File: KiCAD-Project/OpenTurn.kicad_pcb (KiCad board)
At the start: 4 copper layers, 90 x 90 mm, 152 parts, among them J201 XT30, J202 XT30, J203 TLE2, J204 CAN, J205 CAN, J301 GPIOs, J302 JTAG/SW, Q501 IAUC120N06S5N017ATMA1, Q502 IAUC120N06S5N017ATMA1, Q601 IAUC120N06S5N017ATMA1, Q602 IAUC120N06S5N017ATMA1, Q701 IAUC120N06S5N017ATMA1, Q702 IAUC120N06S5N017ATMA1, U201 TI_TCAN337G, U202 TLE5012B_E1000, U203 MAX15062A, U301 CY8C6244AZI-S4D92, U302 MCP9700AT-HTT, U303 MCP9700AT-HTT, U401 DRV8323SRTAR-DRV8323SRTAR, Y301 32MHz

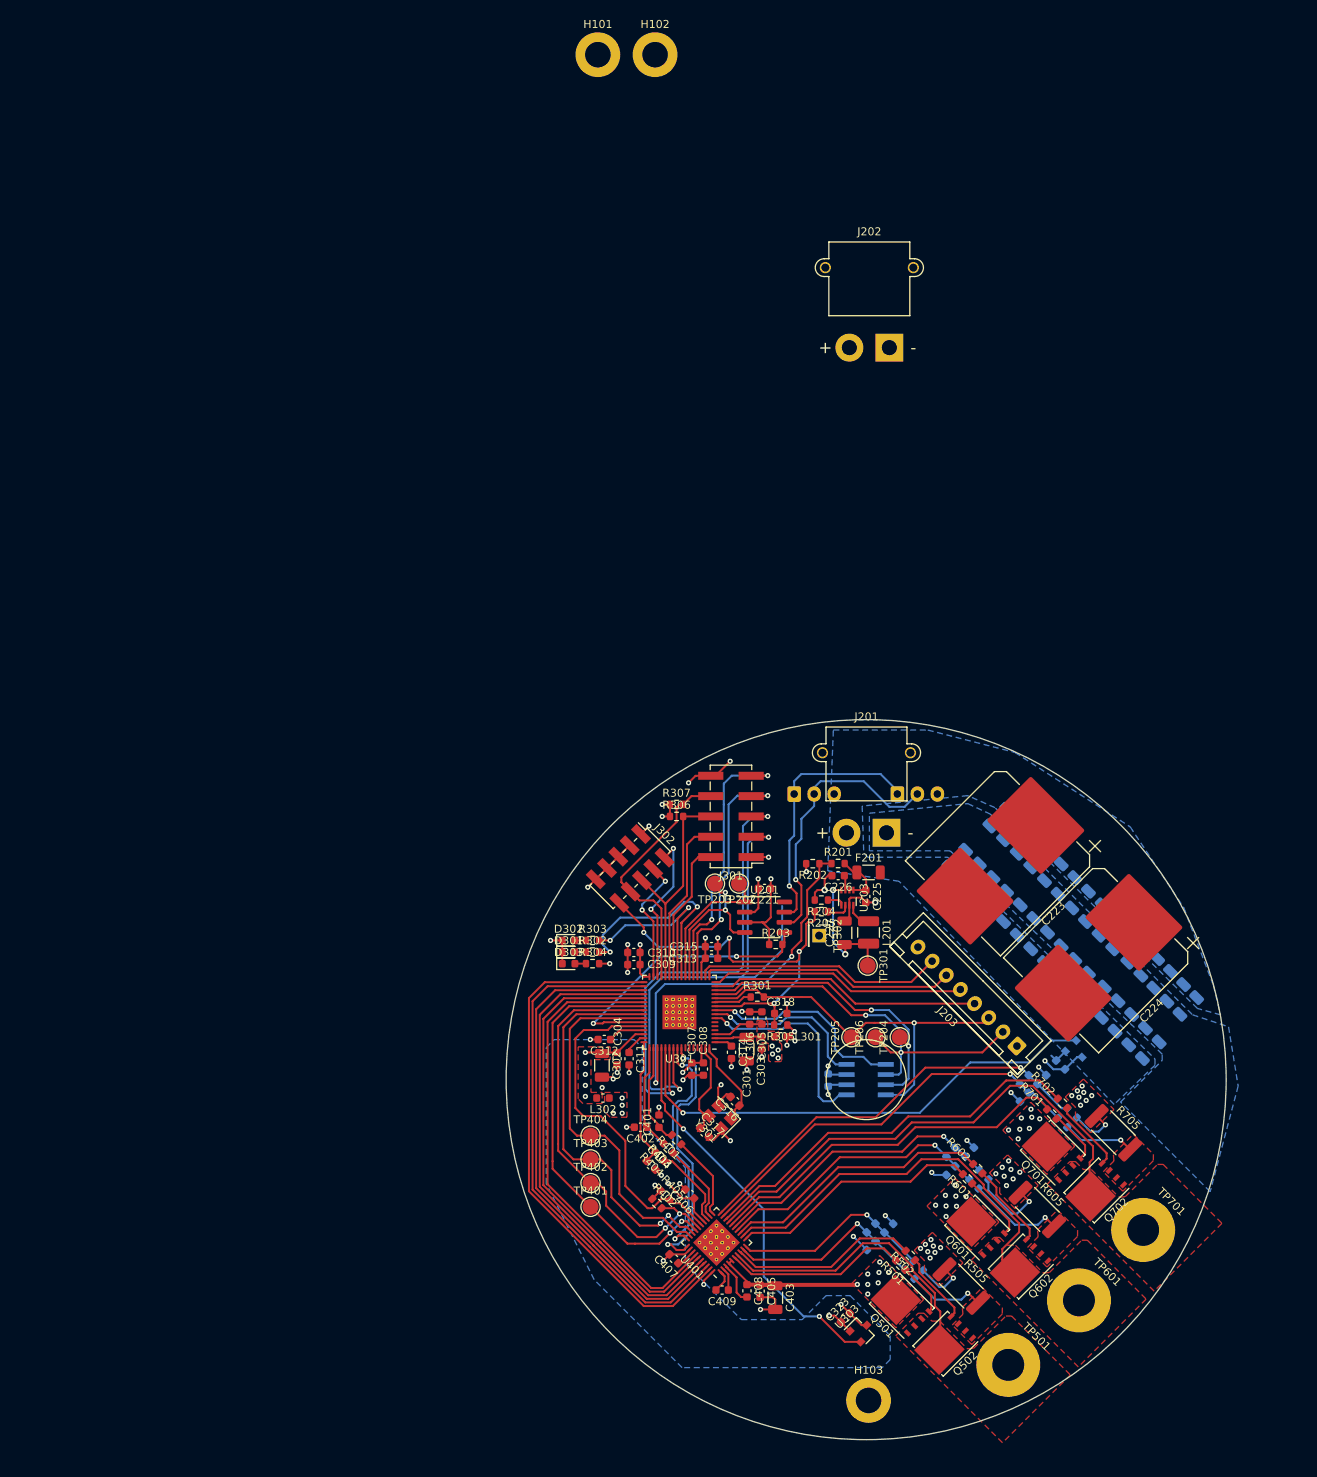
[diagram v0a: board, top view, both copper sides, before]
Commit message: layout redesign started
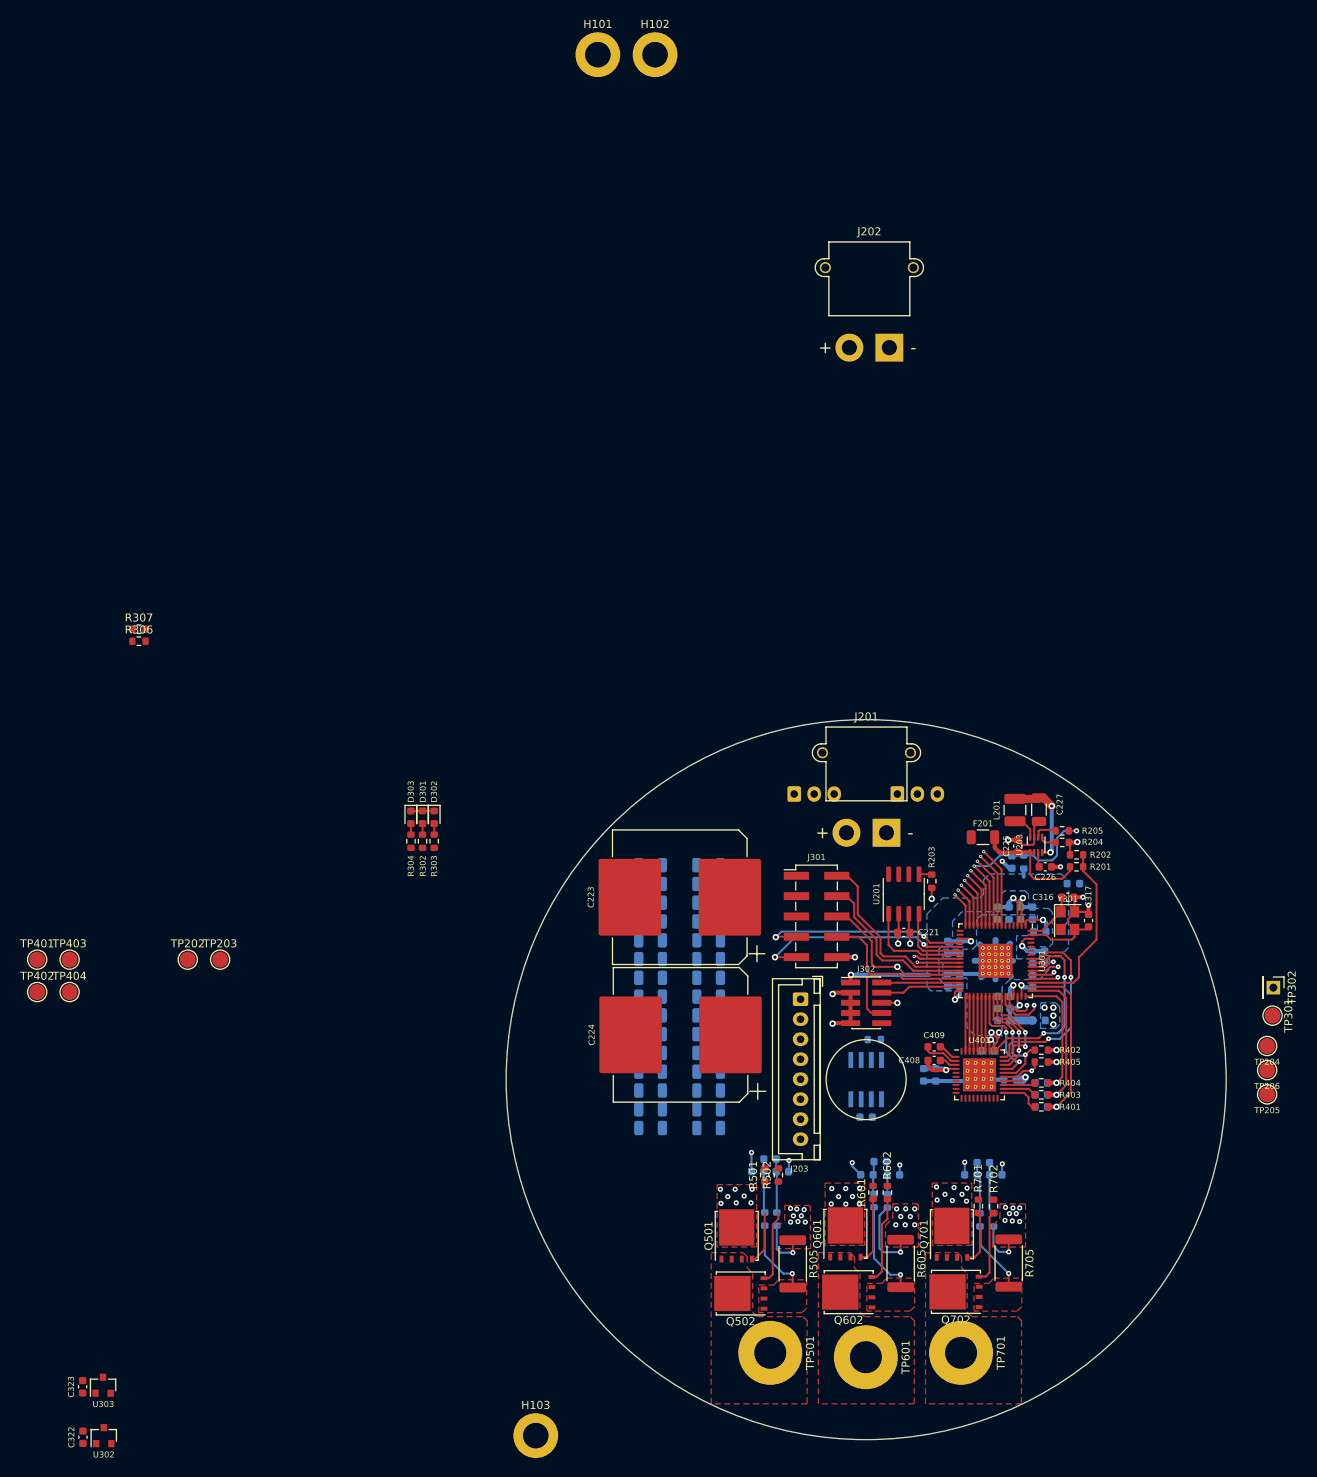
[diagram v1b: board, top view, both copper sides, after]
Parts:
- C301, C302, C403: footprint Capacitor_SMD:C_1206_3216Metric -> Capacitor_SMD:C_0603_1608Metric; moved to B.Cu
- C303, C304, C305, C306, C307, C308, C309, C310, C311, C312, C313, C314, C315, C318, C401, C402, C404, C405, C406, C407, L301, L302, R301, R305: moved to B.Cu
- C322, U302: moved to F.Cu
- J302: value JTAG/SW -> JTAG/SWD; footprint Connector_PinHeader_2.00mm:PinHeader_2x05_P2.00mm_Vertical_SMD -> Connector_PinHeader_1.27mm:PinHeader_2x05_P1.27mm_Vertical_SMD
- moved C322 130.8 mm to (29.1, 171.7), turned to 90 degrees
- moved U302 130.7 mm to (31.7, 171.5), turned to 90 degrees
- moved C323 95.7 mm to (29.1, 165.4), turned to 90 degrees
- moved U303 95.0 mm to (31.6, 165.2), turned to 90 degrees
- moved TP401 75.8 mm to (23.4, 112.0)
- moved TP402 73.2 mm to (23.4, 116.0)
- moved R306 70.7 mm to (36.1, 72.2)
- moved R307 70.7 mm to (36.1, 70.7)
- moved TP403 69.7 mm to (27.4, 112.0)
- moved TP202 69.6 mm to (42.2, 112.0), turned to 0 degrees
- moved TP404 67.5 mm to (27.4, 116.0)
- moved C237 63.3 mm to (100.0, 133.0), turned to 0 degrees
- moved TP203 62.6 mm to (46.2, 112.0), turned to 0 degrees
- moved C232 61.9 mm to (107.3, 133.0), turned to 180 degrees
- moved C236 61.5 mm to (100.0, 130.7), turned to 0 degrees
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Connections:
- J302 pad 1: +3V3 -> VDD
- R305 pad 1: +3V3 -> VDD
- U201 pad 8: Net-(U201-Pad8) -> (no net)
- U301 pad 16: /Interfaces/ENCODER_QOAD_A2 -> /Interfaces/ENCODER_QOAD_A1
- U301 pad 17: /Interfaces/ENCODER_QOAD_B2 -> /Interfaces/ENCODER_QOAD_B1
- U301 pad 18: /Interfaces/ENCODER_QOAD_I2 -> /Interfaces/ENCODER_QOAD_I1
- U301 pad 4: Net-(U301-Pad4) -> (no net)
- U301 pad 5: Net-(U301-Pad5) -> (no net)
- U301 pad 56: /MCU/DRV_ENABLE -> /MCU/DRV_CAL
- U301 pad 57: /MCU/DRV_CAL -> /MCU/DRV_ENABLE
- U301 pad 58: Net-(U301-Pad58) -> (no net)
- U301 pad 59: Net-(U301-Pad59) -> (no net)
- U301 pad 6: Net-(U301-Pad6) -> (no net)
- U301 pad 60: Net-(U301-Pad60) -> (no net)
- U301 pad 61: Net-(U301-Pad61) -> (no net)
- U301 pad 7: /Interfaces/ENCODER_QOAD_A1 -> /Interfaces/ENCODER_QOAD_A2
- U301 pad 8: /Interfaces/ENCODER_QOAD_B1 -> /Interfaces/ENCODER_QOAD_B2
- U301 pad 9: /Interfaces/ENCODER_QOAD_I1 -> /Interfaces/ENCODER_QOAD_I2
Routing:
- net /MCU/DRV_PWM_AL: track 69.8 -> 6.88 mm
- net /Power/sheet6171E233/FET_HS: track 62.2 -> 0.00 mm
- net /MCU/DRV_PWM_AH: track 67.8 -> 6.88 mm
- net /MCU/TEMP2: track 61.9 -> 3.00 mm
- net /MCU/DRV_PWM_BL: track 65.4 -> 6.88 mm
- net /MCU/DRV_PWM_BH: track 63.2 -> 6.88 mm
- net /MCU/DRV_PWM_CL: track 61.1 -> 6.88 mm
- net /MCU/DRV_PWM_CH: track 59.0 -> 6.88 mm
- net /Power/sheet617091A8/FET_HS: track 49.7 -> 0.00 mm
- net /Power/sheet6171E233/FET_GL: track 49.6 -> 0.00 mm
- net /Power/sheet6171E233/FET_GH: track 46.7 -> 0.00 mm
- net /Power/sheet6171E233/I_SENSE_N: track 53.0 -> 6.54 mm, vias 1 -> 0
- net /MCU/GPIO3: track 68.4 -> 22.1 mm, vias 2 -> 1
- net /MCU/TEMP1: track 49.4 -> 3.44 mm, vias 2 -> 1
- net /Power/sheet6171E233/I_SENSE_P: track 51.5 -> 6.47 mm, vias 1 -> 0
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- added copper zone on B.Cu, net +3V3
- added copper zone on B.Cu, net VDD
- removed copper zone on F.Cu, net +3V3
- removed copper zone on In2.Cu, net +3V3
- removed copper zone on In1.Cu, net GND
- removed copper zone on B.Cu, net VBUS
- removed copper zone on F.Cu, net VDD
- removed copper zone on In2.Cu, net VDD
- removed copper zone on B.Cu, net VDDA
- removed copper zone on F.Cu, net VDDA
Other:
- net class Default: via_dia 0.8 -> 0.6; via_drill 0.4 -> 0.2
- rule trace_min: 0.1 -> 0.2
- rule via_min_drill: 0.3 -> 0.2

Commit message: pcb update, kicad 5.99
PCB Update for review, moved to KiCad 5.99 nightly build
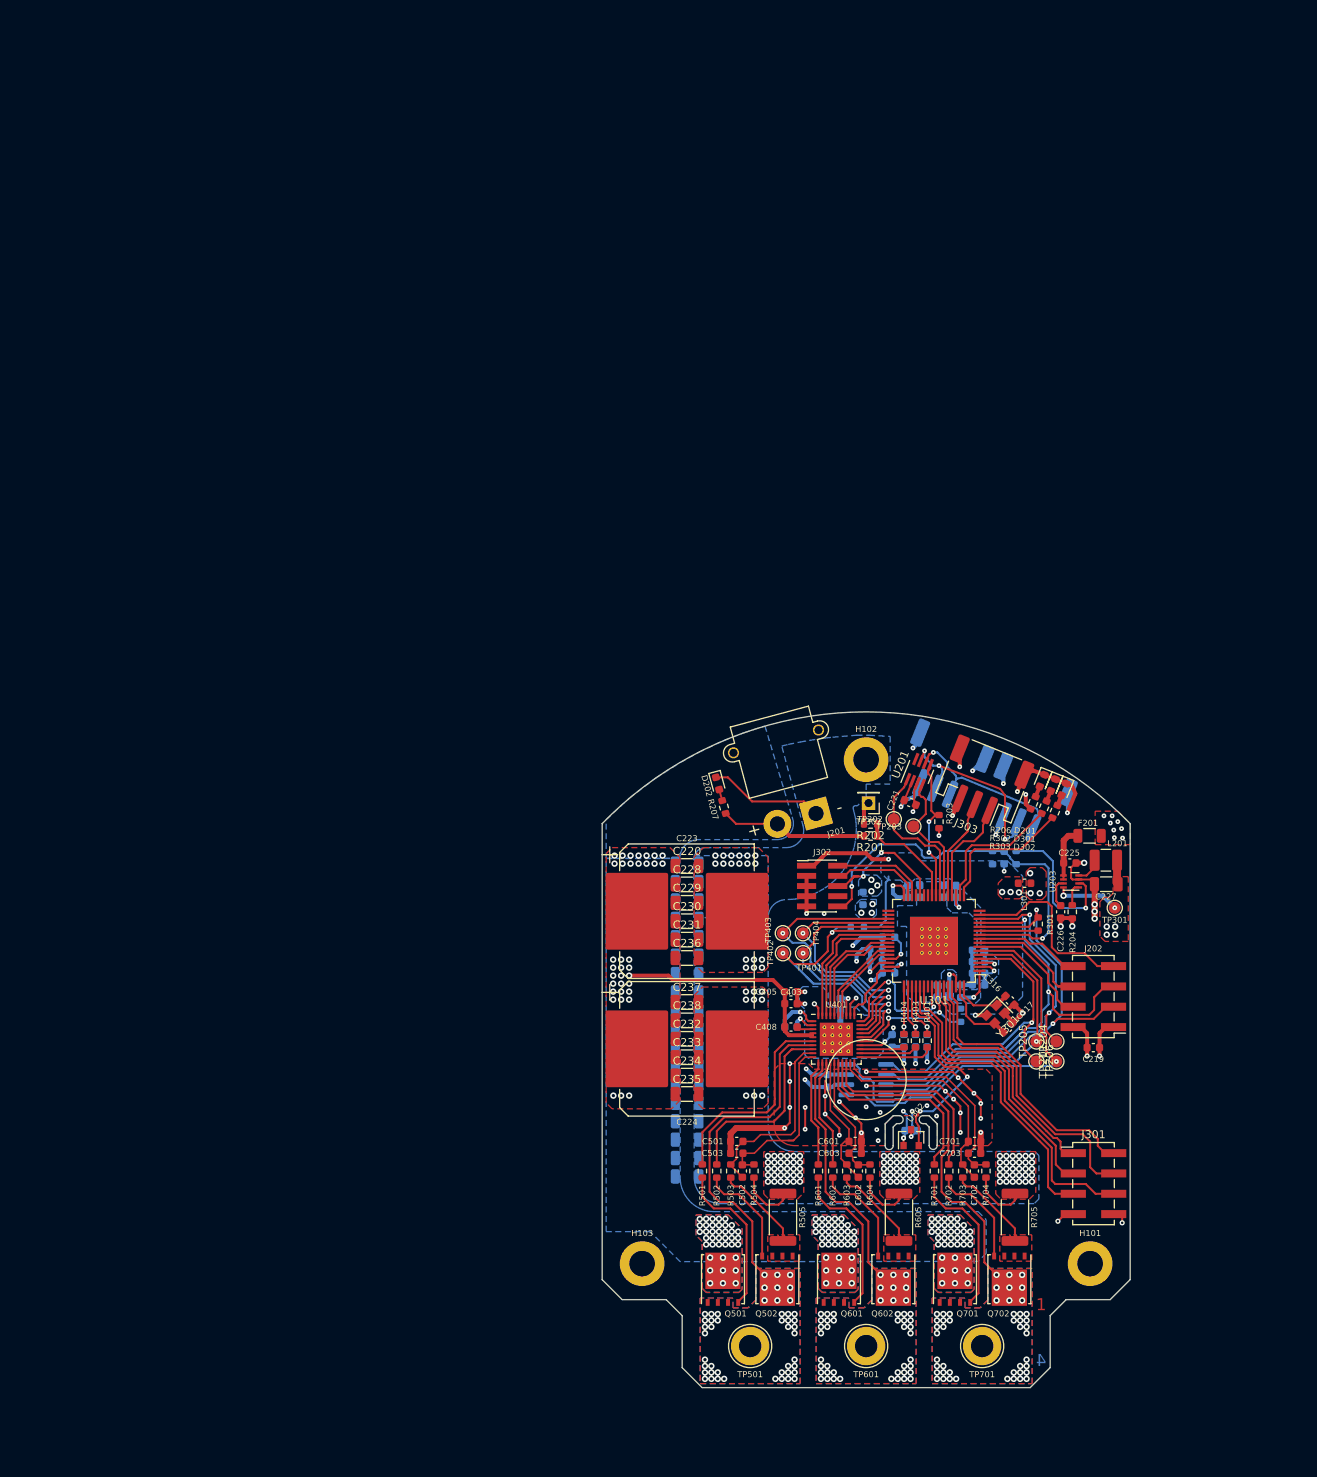
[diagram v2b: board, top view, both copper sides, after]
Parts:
- removed the C322 at (29.1, 171.7)
- removed D303: LED_Small, LED_SMD:LED_0603_1608Metric
- removed the J203 at (118.8, 117.0)
- removed R304, R306, R307: 4k7, Resistor_SMD:R_0603_1608Metric
- removed the U302 at (31.7, 171.5)
- added C238: 10u, Capacitor_SMD:C_1206_3216Metric, F.Cu at (104.6, 119.6)
- added D201: LED_Small, LED_SMD:LED_0603_1608Metric, F.Cu at (149.0, 89.6)
- added D202: LED_Small, LED_SMD:LED_0603_1608Metric, F.Cu at (108.4, 90.0)
- added J303: Conn_01x03_Shielded, Connector_JST:JST_PH_S3B-PH-SM4-TB_1x03-1MP_P2.00mm_Horizontal, F.Cu at (141.7, 90.0)
- added R206: 4k7, Resistor_SMD:R_0603_1608Metric, F.Cu at (147.9, 92.4)
- added R207: 4k7, Resistor_SMD:R_0603_1608Metric, F.Cu at (109.2, 92.9)
- added TP201: TLE_CSQ, TestPoint:TestPoint_Pad_D1.5mm, F.Cu at (150.8, 124.7)
- C219: value 10u -> 1u; footprint Capacitor_SMD:C_1206_3216Metric -> Capacitor_SMD:C_0603_1608Metric; moved to F.Cu
- C220, C228, C229, C230, C231, C232, C233, C234, C235, C236, C237, C403, C405, C501, C502, C503, C601, C602, C603, C701, C702, C703, L301, R301, R503, R504, R603, R604, R703, R704: moved to F.Cu
- C322: renamed from C323; moved to B.Cu
- C409, R205, R402, R405: moved to B.Cu
- J202: value XT30 -> Conn_02x04_Odd_Even; footprint Connector_AMASS:AMASS_XT30PW-M_1x02_P2.50mm_Horizontal -> Connector_PinHeader_2.54mm:PinHeader_2x04_P2.54mm_Vertical_SMD
- J203: renamed from J205; value CAN -> Conn_01x03_Shielded; footprint Connector_JST:JST_XH_S3B-XH-A_1x03_P2.50mm_Horizontal -> Connector_JST:JST_PH_S3B-PH-SM4-TB_1x03-1MP_P2.00mm_Horizontal
- J204: value CAN -> Conn_01x03_Shielded; footprint Connector_JST:JST_XH_S3B-XH-A_1x03_P2.50mm_Horizontal -> Connector_JST:JST_PH_S3B-PH-SM4-TB_1x03-1MP_P2.00mm_Horizontal
- J301: footprint Connector_PinHeader_2.54mm:PinHeader_2x05_P2.54mm_Vertical_SMD -> Connector_PinHeader_2.54mm:PinHeader_2x04_P2.54mm_Vertical_SMD
- R505, R605, R705: value 0.05m -> 5mR
- TP202, TP203, TP204, TP205, TP206, TP301: footprint TestPoint:TestPoint_Pad_D2.0mm -> TestPoint:TestPoint_Pad_D1.5mm
- TP401: renamed from TP402; value MISO -> MOSI; footprint TestPoint:TestPoint_Pad_D2.0mm -> TestPoint:TestPoint_Pad_D1.5mm
- TP402: renamed from TP404; value DRV_CS -> MISO; footprint TestPoint:TestPoint_Pad_D2.0mm -> TestPoint:TestPoint_Pad_D1.5mm
- TP403: renamed from TP401; value MOSI -> SPI_SCK; footprint TestPoint:TestPoint_Pad_D2.0mm -> TestPoint:TestPoint_Pad_D1.5mm
- TP404: renamed from TP403; value SPI_SCK -> DRV_CS; footprint TestPoint:TestPoint_Pad_D2.0mm -> TestPoint:TestPoint_Pad_D1.5mm
- TP501, TP601, TP701: footprint MountingHole:MountingHole_4mm_Pad -> TestPoint:TestPoint_Loop_D3.80mm_Drill2.8mm
- U201: footprint Package_SO:SOIC-8_3.9x4.9mm_P1.27mm -> Package_TO_SOT_SMD:SOT-23-8_Handsoldering
- U202: footprint digikey-footprints:SOIC-8_W3.9mm -> Package_SO:SOIC-8_3.9x4.9mm_P1.27mm
- U301: footprint Package_DFN_QFN:Texas_S-PVQFN-N64_EP4.25x4.25mm_ThermalVias -> Package_QFP:HTQFP-64-1EP_10x10mm_P0.5mm_EP8x8mm_Mask4.4x4.4mm_ThermalVias
- Y301: footprint Crystal:Crystal_SMD_3225-4Pin_3.2x2.5mm -> Crystal:Crystal_SMD_2520-4Pin_2.5x2.0mm
- moved H101 163.2 mm to (155.0, 150.0)
- moved C322 108.4 mm to (132.6, 133.4), turned to 0 degrees
- moved U302 105.6 mm to (132.6, 134.2)
- moved TP401 95.9 mm to (119.1, 111.2), turned to 90 degrees
- moved TP403 93.3 mm to (116.6, 108.7)
- moved H102 92.0 mm to (127.0, 87.0)
- moved TP404 91.7 mm to (119.1, 108.7), turned to -90 degrees
- moved TP202 90.0 mm to (130.4, 94.5), turned to 70 degrees
- moved TP402 89.3 mm to (116.6, 111.2), turned to -90 degrees
- moved TP203 88.2 mm to (132.9, 95.3), turned to 70 degrees
- moved J202 85.0 mm to (155.4, 116.6), turned to 180 degrees
- moved D301 78.9 mm to (150.4, 90.2), turned to -112 degrees
- moved D302 78.8 mm to (151.7, 90.7), turned to -112 degrees
- moved R302 77.8 mm to (149.3, 93.0), turned to -112 degrees
- moved R303 77.7 mm to (150.6, 93.5), turned to -112 degrees
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- renumbered U303 to U302
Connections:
- net /Interfaces/RESET renamed /MCU/RESET
- net /MCU/SWDCLK_TCKL renamed /MCU/SWDCLK
- net /MCU/SWDIO_TMS renamed /MCU/SWDIO
- C219 pad 1: VBUS -> +3V3
- C219 pad 2: GND -> GNDS
- C221 pad 2: GND -> GNDS
- C222 pad 2: GND -> GNDS
- C225 pad 2: GND -> GNDS
- C226 pad 2: GND -> GNDS
- C227 pad 2: GND -> GNDS
- C301 pad 2: GND -> GNDS
- C302 pad 2: GND -> GNDA
- C303 pad 2: GND -> GNDS
- C304 pad 2: GND -> GNDA
- C305 pad 2: GND -> GNDS
- C306 pad 2: GND -> GNDS
- C307 pad 2: GND -> GNDS
- C308 pad 2: GND -> GNDS
- C309 pad 2: GND -> GNDS
- C310 pad 2: GND -> GNDS
- C311 pad 2: GND -> GNDA
- C312 pad 2: GND -> GNDA
- C313 pad 2: GND -> GNDS
- C314 pad 2: GND -> GNDS
- C315 pad 2: GND -> GNDS
- C316 pad 2: GND -> GNDS
- C317 pad 2: GND -> GNDS
- C318 pad 2: GND -> GNDS
- C322 pad 2: GND -> GNDA
- C401 pad 2: GND -> GNDA
- C402 pad 2: GND -> GNDA
- C404 pad 2: GND -> GNDA
- C406 pad 2: GND -> GNDA
- C501 pad 2: GND -> GNDA
- C503 pad 2: GND -> GNDA
- C601 pad 2: GND -> GNDA
- C603 pad 2: GND -> GNDA
- C701 pad 2: GND -> GNDA
- C703 pad 2: GND -> GNDA
- D301 pad 1: GND -> GNDS
- D302 pad 1: GND -> GNDS
- H101 pad 1: GND -> GNDS
- H103 pad 1: GND -> unconnected-(H103-Pad1)
- J202 pad 1: GND -> +3V3
- J202 pad 2: VBUS -> GNDS
- J203 pad 1: Net-(J204-Pad1) -> GNDS
- J203 pad 2: Net-(J204-Pad2) -> Net-(J203-Pad2)
- J203 pad 3: GND -> Net-(J203-Pad3)
- J204 pad 1: Net-(J204-Pad1) -> GNDS
- J204 pad 2: Net-(J204-Pad2) -> Net-(J203-Pad2)
- J204 pad 3: GND -> Net-(J203-Pad3)
- J301 pad 1: +3V3 -> /MCU/GPIO0
- J301 pad 2: /MCU/GPIO0 -> /MCU/GPIO1
- J301 pad 3: /MCU/GPIO3 -> /MCU/GPIO2
- J301 pad 4: /MCU/GPIO1 -> /MCU/GPIO3
- J301 pad 5: /MCU/GPIO2 -> /MCU/GPIO4
- J301 pad 6: /MCU/SWO_TDO_SCL -> /MCU/GPIO5
- J301 pad 7: /MCU/DEBUG_UART_RX -> +3V3
- J301 pad 8: /MCU/TDI_SDA -> GNDS
- J302 pad 3: GND -> GNDS
- J302 pad 5: GND -> GNDS
- J302 pad 6: /MCU/SWO_TDO_SCL -> /MCU/SWO
- J302 pad 7: GND -> GNDS
- J302 pad 8: /MCU/TDI_SDA -> unconnected-(J302-Pad8)
- J302 pad 9: GND -> GNDS
- R201 pad 2: Net-(C225-Pad1) -> VBUS
- R202 pad 2: GND -> GNDS
- R204 pad 2: GND -> GNDS
- R302 pad 2: /MCU/STATUS_LED0 -> /MCU/STATUS_LED1
- R303 pad 2: /MCU/STATUS_LED1 -> /MCU/STATUS_LED0
- R402 pad 1: +3V3 -> VDD
- R405 pad 1: +3V3 -> VDD
- TP205 pad 1: /Interfaces/ENCODER_DATA -> /Interfaces/ENCODER_QOAD_B1
- TP206 pad 1: /Interfaces/ENCODER_SCK -> /Interfaces/ENCODER_QOAD_I1
- TP302 pad 1: GND -> GNDS
- TP401 pad 1: /MCU/DRV_MISO -> /MCU/DRV_MOSI
- TP402 pad 1: /MCU/DRV_CS -> /MCU/DRV_MISO
- TP403 pad 1: /MCU/DRV_MOSI -> /MCU/DRV_SCK
- TP404 pad 1: /MCU/DRV_SCK -> /MCU/DRV_CS
- U201 pad 2: GND -> GNDS
- U201 pad 6: Net-(J204-Pad2) -> Net-(J203-Pad3)
- U201 pad 7: Net-(J204-Pad1) -> Net-(J203-Pad2)
- U201 pad 8: (no net) -> unconnected-(U201-Pad8)
- U202 pad 7: GND -> GNDS
- U203 pad 7: GND -> GNDS
- U301 pad 16: /Interfaces/ENCODER_QOAD_A1 -> unconnected-(U301-Pad16)
- U301 pad 17: /Interfaces/ENCODER_QOAD_B1 -> /MCU/STATUS_LED0
- U301 pad 18: /Interfaces/ENCODER_QOAD_I1 -> /MCU/STATUS_LED1
- U301 pad 24: /MCU/STATUS_LED0 -> /Interfaces/CANFD_Fault
- U301 pad 25: /MCU/STATUS_LED1 -> /Interfaces/V_BUS_SENSE
- U301 pad 26: /MCU/GPIO0 -> unconnected-(U301-Pad26)
- U301 pad 27: /MCU/GPIO1 -> unconnected-(U301-Pad27)
- U301 pad 28: /MCU/SWO_TDO_SCL -> /MCU/SWO
- U301 pad 29: /MCU/TDI_SDA -> unconnected-(U301-Pad29)
- U301 pad 33: /MCU/DRV_PWM_AL -> unconnected-(U301-Pad33)
- U301 pad 34: /MCU/DRV_PWM_AH -> unconnected-(U301-Pad34)
- U301 pad 35: /MCU/DRV_PWM_BL -> /MCU/DRV_SCK
- U301 pad 36: /MCU/DRV_PWM_BH -> /MCU/DRV_CS
- U301 pad 37: /MCU/DRV_PWM_CL -> /MCU/DRV_MOSI
- U301 pad 38: /MCU/DRV_PWM_CH -> /MCU/DRV_MISO
- U301 pad 39: /MCU/DRV_MOSI -> /MCU/DRV_PWM_AL
- U301 pad 4: (no net) -> /Interfaces/ENCODER_QOAD_I1
- U301 pad 40: /MCU/DRV_MISO -> /MCU/DRV_PWM_AH
- U301 pad 41: /MCU/DRV_SCK -> /MCU/DRV_PWM_BL
- U301 pad 42: /MCU/DRV_CS -> /MCU/DRV_PWM_BH
- U301 pad 43: /Interfaces/CANFD_Fault -> /MCU/DRV_PWM_CL
- U301 pad 44: /MCU/DRV_nFAULT -> /MCU/DRV_PWM_CH
- U301 pad 48: /MCU/DRV_ISENSE_A -> /MCU/DRV_CAL
- U301 pad 49: /MCU/DRV_ISENSE_B -> /MCU/DRV_ISENSE_A
- U301 pad 5: (no net) -> /Interfaces/ENCODER_QOAD_B1
- U301 pad 50: /MCU/DRV_ISENSE_C -> /MCU/DRV_ISENSE_B
- U301 pad 51: /Interfaces/V_BUS_SENSE -> /MCU/DRV_ISENSE_C
- U301 pad 53: /MCU/TEMP2 -> /MCU/GPIO4
- U301 pad 54: /MCU/GPIO2 -> /MCU/GPIO5
- U301 pad 55: /MCU/GPIO3 -> unconnected-(U301-Pad55)
- U301 pad 56: /MCU/DRV_CAL -> /MCU/DRV_ENABLE
- U301 pad 57: /MCU/DRV_ENABLE -> /MCU/DRV_nFAULT
- U301 pad 58: (no net) -> /MCU/GPIO2
- U301 pad 59: (no net) -> /MCU/GPIO0
- U301 pad 6: (no net) -> /Interfaces/ENCODER_QOAD_A1
- U301 pad 60: (no net) -> /MCU/GPIO3
- U301 pad 61: (no net) -> /MCU/GPIO1
- U301 pad 65: GND -> GNDS
- U302 pad 3: GND -> GNDA
- U401 pad 32: GND -> GNDA
- Y301 pad 2: GND -> GNDS
- Y301 pad 4: GND -> GNDS
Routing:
- net GNDS: track 0.00 -> 109.8 mm, vias 0 -> 23
- net GNDA: track 0.00 -> 97.5 mm, vias 0 -> 37
- net GND: track 120.1 -> 46.3 mm, vias 45 -> 120
- net /Interfaces/ENCODER_DATA: track 6.92 -> 58.8 mm, vias 1 -> 2
- net /Interfaces/ENCODER_SCK: track 6.30 -> 57.9 mm, vias 1 -> 2
- net /Interfaces/ENCODER_QOAD_B1: track 0.00 -> 46.7 mm, vias 0 -> 1
- net /Interfaces/ENCODER_QOAD_A1: track 4.35 -> 50.1 mm
- net /Interfaces/ENCODER_CS0: track 5.63 -> 49.4 mm, vias 1 -> 2
- net /MCU/GPIO5: track 0.00 -> 43.6 mm
- net /Power/Sheet61668C54/FET_HS: track 0.00 -> 43.0 mm, vias 0 -> 47
- net /Power/sheet6171E233/FET_HS: track 0.00 -> 42.2 mm, vias 0 -> 47
- net VBUS: track 7.31 -> 47.8 mm, vias 25 -> 160
- net /Interfaces/ENCODER_QOAD_I1: track 0.00 -> 40.1 mm, vias 0 -> 1
- net /MCU/GPIO4: track 0.00 -> 39.2 mm
- net +3V3: track 24.1 -> 62.4 mm, vias 10 -> 18
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- added copper zone on F.Cu, net +3V3
- added copper zone on In2.Cu, net +3V3
- added copper zone on B.Cu, net /Power/Sheet61668C54/FET_HS
- added copper zone on In1.Cu, net /Power/Sheet61668C54/FET_HS
- added copper zone on In2.Cu, net /Power/Sheet61668C54/FET_HS
- added copper zone on B.Cu, net /Power/sheet617091A8/FET_HS
- added copper zone on In1.Cu, net /Power/sheet617091A8/FET_HS
- added copper zone on In2.Cu, net /Power/sheet617091A8/FET_HS
- added copper zone on B.Cu, net /Power/sheet6171E233/FET_HS
- added copper zone on In1.Cu, net /Power/sheet6171E233/FET_HS
- added copper zone on In2.Cu, net /Power/sheet6171E233/FET_HS
- added copper zone on In1.Cu, net GND
- added copper zone on In2.Cu, net GND
- added copper zone on F.Cu, net GNDA
- added copper zone on In1.Cu, net GNDA
- added copper zone on B.Cu, net GNDS
- added copper zone on In1.Cu, net GNDS
- added copper zone on B.Cu, net VBUS
- added copper zone on In1.Cu, net VBUS
- added copper zone on In2.Cu, net VBUS
- added copper zone on F.Cu, net VDD
- added copper zone on B.Cu, net VDDA
- added copper zone on In2.Cu, net VDDA
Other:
- board size 90 x 90 mm -> 66 x 84.5 mm
- net class Default removed
- rule pad_to_mask_clearance: 0 -> 0.05
- board text added: "1"
- board text added: "2"
- board text added: "3"
- board text added: "4"

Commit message: started fixing DRC errors
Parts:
- moved R704 0.08 mm to (142.1, 138.4)
- moved R504 0.08 mm to (113.0, 138.4)
- moved R604 0.08 mm to (127.5, 138.4)
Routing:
- net /MCU/STATUS_LED1: track 17.3 -> 18.3 mm
- net /MCU/STATUS_LED0: track 17.7 -> 18.7 mm
- net VDDA: vias 10 -> 9
